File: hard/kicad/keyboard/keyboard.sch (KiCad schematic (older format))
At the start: 95 parts, among them J1 IOx, J2 IOx, J3 IOx, SW01 Space, SW02 <, SW04 Tab, SW08 º \\, SW101 Space, SW11 Z, SW12 A, SW14 Q, SW18 1, SW1F1 Alt, SW1F2 Control, SW1F4 Shift, SW201 Space, SW21 X, SW22 S, SW24 W, SW28 2, SW31 C, SW32 D, SW34 E, SW38 3, SW41 V, SW42 F, SW44 R, SW48 4, SW51 B, SW52 G, SW54 T, SW58 5, SW61 N, SW62 H, SW64 Y, SW68 6, SW71 M, SW72 J, SW74 U, SW78 7, SW81 ,, SW82 K, SW84 I, SW88 8, SW91 ., SW92 L, SW94 O, SW98 9, U1 74HC154, U2 74HC174

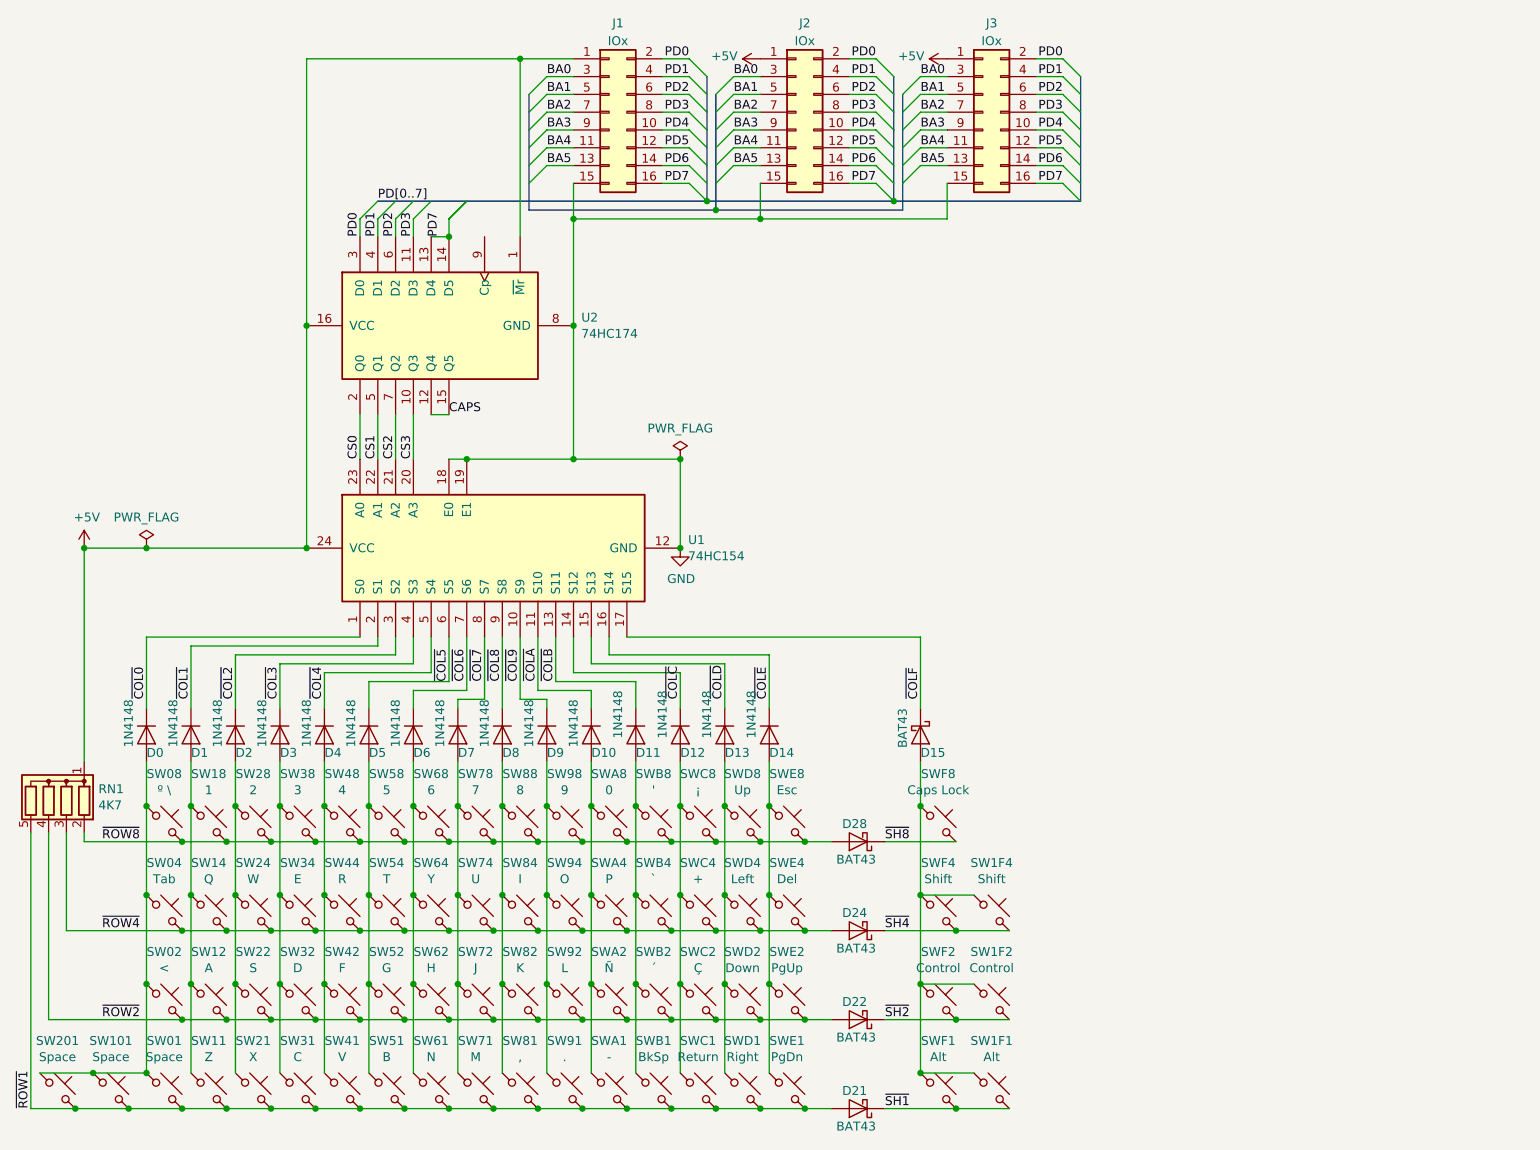
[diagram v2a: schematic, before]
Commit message: final values for keyboard
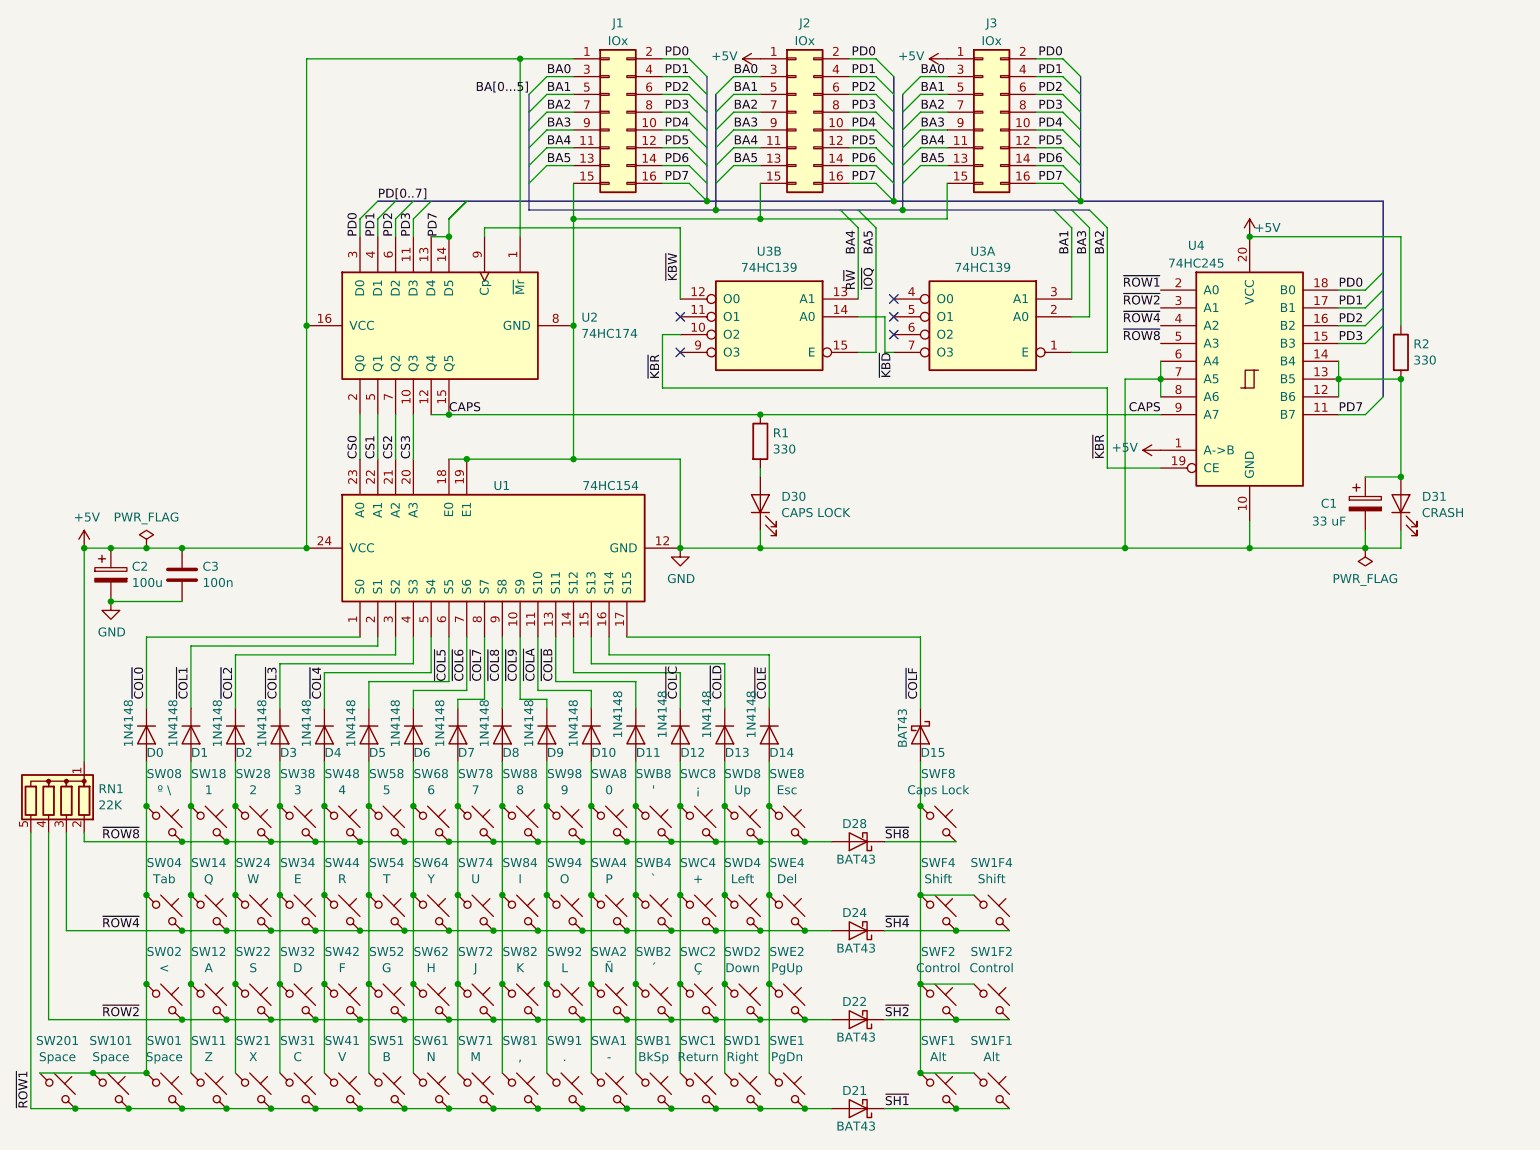
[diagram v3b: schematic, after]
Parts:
- added C1: 33 uF, Capacitor_THT:CP_Radial_D6.3mm_P2.50mm, symbol Device:CP
- added C2: 100u, Capacitor_THT:CP_Radial_D6.3mm_P2.50mm, symbol Device:CP
- added C3: 100n, Capacitor_THT:C_Rect_L7.2mm_W2.5mm_P5.00mm_FKS2_FKP2_MKS2_MKP2, symbol Device:C
- added D30: CAPS LOCK, LED_THT:LED_D3.0mm, symbol Device:LED
- added D31: CRASH, LED_THT:LED_D3.0mm, symbol Device:LED
- added R1, R2: 330, Resistor_THT:R_Axial_DIN0207_L6.3mm_D2.5mm_P10.16mm_Horizontal, symbol Device:R
- added U3: 74HC139, Package_DIP:DIP-16_W7.62mm_Socket, symbol 74xx:74LS139
- added U4: 74HC245, Package_DIP:DIP-20_W7.62mm, symbol 74xx:74HC245
- J1, J2, J3: footprint (none) -> Connector_IDC:IDC-Header_2x08_P2.54mm_Vertical
- RN1: value 4K7 -> 22K
- U2: footprint (none) -> Package_DIP:DIP-16_W7.62mm_Socket
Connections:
- net +5V: now also C2.1, C3.1, R2.1, U4.1 (A->B), U4.20 (VCC)
- net BA1: now also U3.3 (A1)
- net BA2: now also U3.1 (E)
- net BA3: now also U3.2 (A0)
- net BA4: now also U3.13 (A1)
- net BA5: now also U3.15 (E)
- net CAPS: now also R1.1, U4.9 (A7)
- net GND: now also C1.2, C2.2, C3.2, D30.1 (K), D31.1 (K), U4.10 (GND), U4.6 (A4), U4.7 (A5), U4.8 (A6)
- net PD0: now also U4.18 (B0)
- net PD1: now also U4.17 (B1)
- net PD2: now also U4.16 (B2)
- net PD3: now also U4.15 (B3)
- net PD7: now also U4.11 (B7)
- net ~ROW1: now also U4.2 (A0)
- net ~ROW2: now also U4.3 (A1)
- net ~ROW4: now also U4.4 (A2)
- net ~ROW8: now also U4.5 (A3)
- net ~KBW: now reaches U2.9 (Cp)
- net ~KBW: now also U3.12 (O0)
- new net: C1.1, D31.2 (A), R2.2, U4.12 (B6), U4.13 (B5), U4.14 (B4)
- new net: D30.2 (A), R1.2
- new net ~KBD: U3.14 (A0), U3.7 (O3)
- new net ~KBR: U3.10 (O2), U4.19 (CE)
- no-connect marks 0 -> 5

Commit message: preliminary ASCII keyboard layout
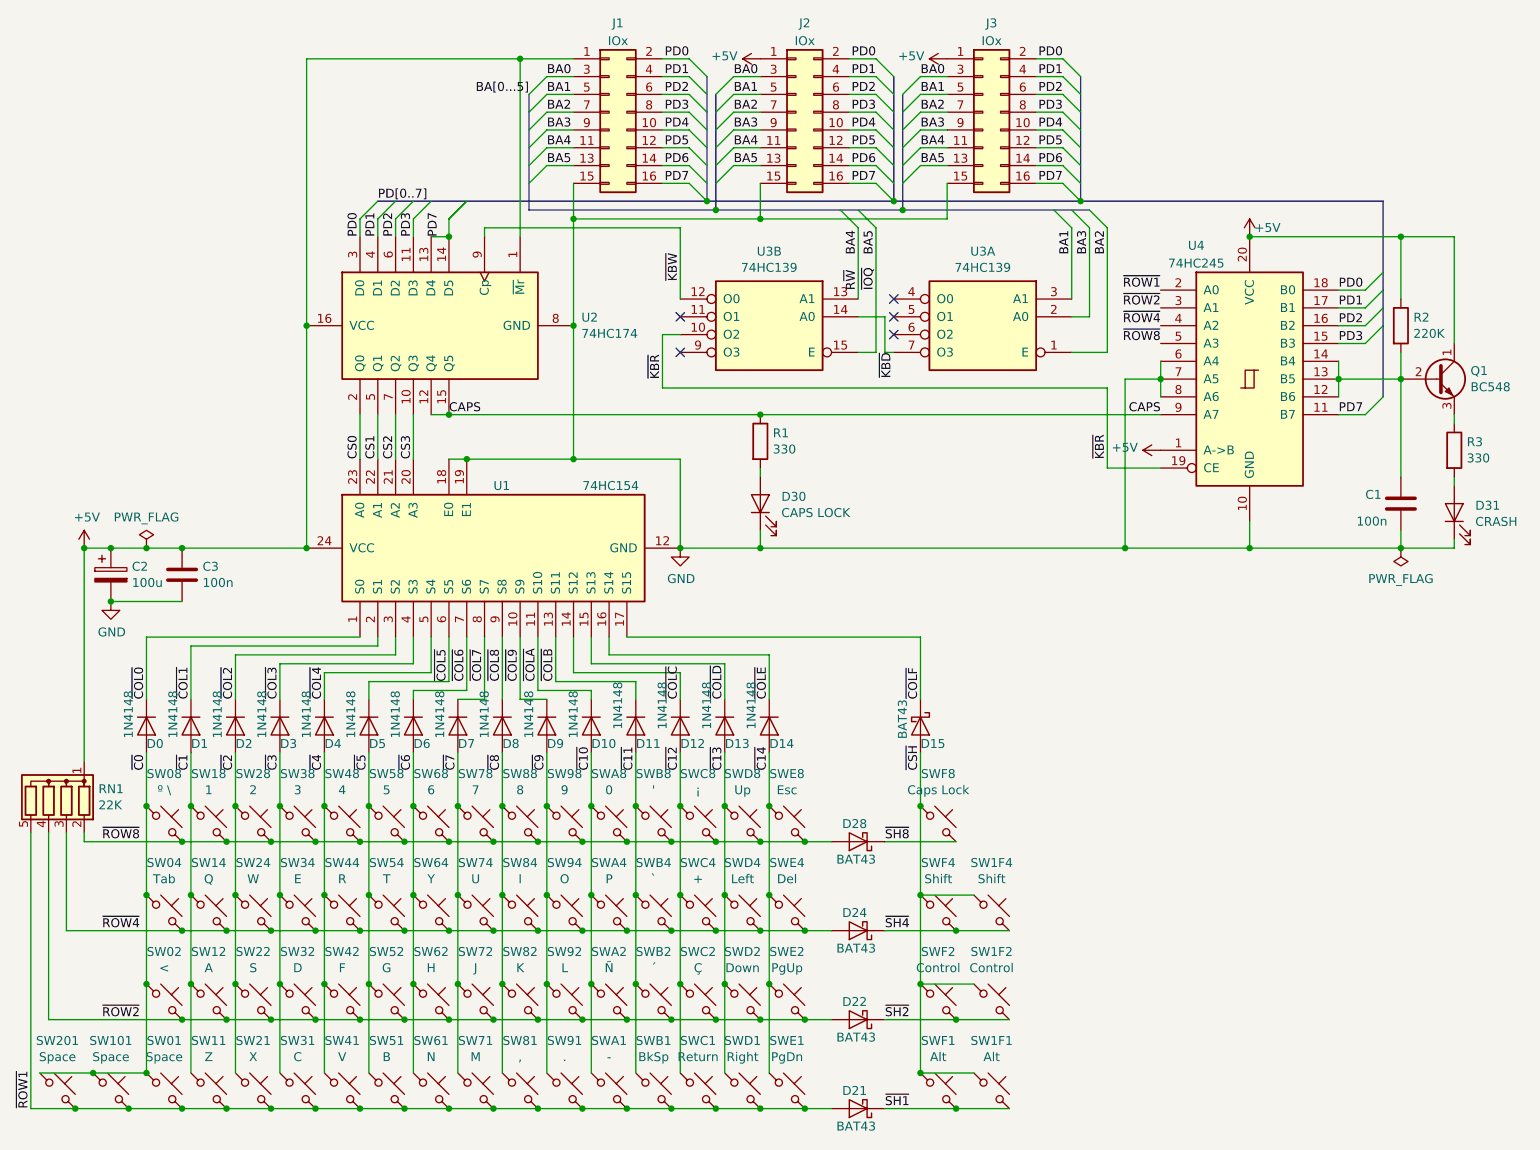
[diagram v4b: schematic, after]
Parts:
- removed C1: 33 uF, Capacitor_THT:CP_Radial_D6.3mm_P2.50mm, symbol Device:CP
- added C1: 100n, Capacitor_THT:C_Rect_L7.2mm_W2.5mm_P5.00mm_FKS2_FKP2_MKS2_MKP2, symbol Device:C
- added Q1: BC548, Package_TO_SOT_THT:TO-92_Inline, symbol Transistor_BJT:BC548
- added R3: 330, Resistor_THT:R_Axial_DIN0207_L6.3mm_D2.5mm_P10.16mm_Horizontal, symbol Device:R
- R2: value 330 -> 220K
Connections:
- net +5V: now also Q1.1 (C)
- net GND: now also C1.2
- net ~C0: now reaches D0.2 (A), SW01.1, SW02.1, SW04.1, SW08.1, SW101.1, SW201.1
- net ~C1: now reaches D1.2 (A), SW11.1, SW12.1, SW14.1, SW18.1
- net ~C2: now reaches D2.2 (A), SW21.1, SW22.1, SW24.1, SW28.1
- net ~C3: now reaches D3.2 (A), SW31.1, SW32.1, SW34.1, SW38.1
- net ~C4: now reaches D4.2 (A), SW41.1, SW42.1, SW44.1, SW48.1
- net ~C5: now reaches D5.2 (A), SW51.1, SW52.1, SW54.1, SW58.1
- net ~C6: now reaches D6.2 (A), SW61.1, SW62.1, SW64.1, SW68.1
- net ~C7: now reaches D7.2 (A), SW71.1, SW72.1, SW74.1, SW78.1
- net ~C8: now reaches D8.2 (A), SW81.1, SW82.1, SW84.1, SW88.1
- net ~C9: now reaches D9.2 (A), SW91.1, SW92.1, SW94.1, SW98.1
- net ~C10: now reaches D10.2 (A), SWA1.1, SWA2.1, SWA4.1, SWA8.1
- net ~C11: now reaches D11.2 (A), SWB1.1, SWB2.1, SWB4.1, SWB8.1
- net ~C12: now reaches D12.2 (A), SWC1.1, SWC2.1, SWC4.1, SWC8.1
- net ~C13: now reaches D13.2 (A), SWD1.1, SWD2.1, SWD4.1, SWD8.1
- net ~C14: now reaches D14.2 (A), SWE1.1, SWE2.1, SWE4.1, SWE8.1
- net ~CSH: now reaches D15.2 (A), SW1F1.1, SW1F2.1, SW1F4.1, SWF1.1, SWF2.1, SWF4.1, SWF8.1
- net at R2.2, U4.12 (B6), U4.13 (B5)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: now also C1.1, Q1.2 (B); no longer D31.2 (A)
- new net: D31.2 (A), R3.2
- new net: Q1.3 (E), R3.1
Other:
- moved on the sheet: D0, D1, D10, D11, D12, D13, D14, D15, D2, D3, D31, D4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
